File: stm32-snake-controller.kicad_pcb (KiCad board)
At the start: 4 copper layers, 100 x 72 mm, 84 parts, among them J101 Barrel_Jack_MountingPin, J102 Tag Connector, J103 JST 2.54 Header, J301 Conn_01x03, J302 Conn_01x03, J401 Conn_01x07, J402 Conn_01x07, J501 USB_A, J601 8P8C_LED_Shielded, Q101 AO3501A, SW101 SW_SPDT, SW102 SW_Push, U101 USBLC6-2SC6, U102 M24C64-RMN, U103 STM32F446RCTx, U201 XC6220B331MR-G, U301 74AHCT1G125, U302 74AHCT1G125, U501 STMPS2141STR, U601 PCA9615DP, Y101 32.768kHz, Y102 16MHz

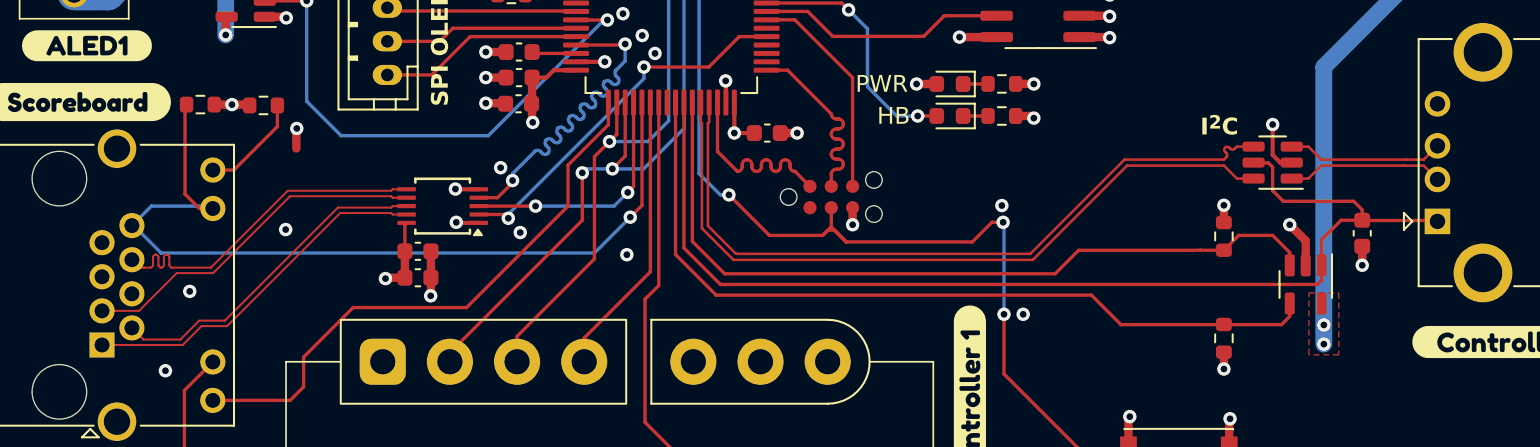
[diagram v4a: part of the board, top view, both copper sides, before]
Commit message: fix differential traces
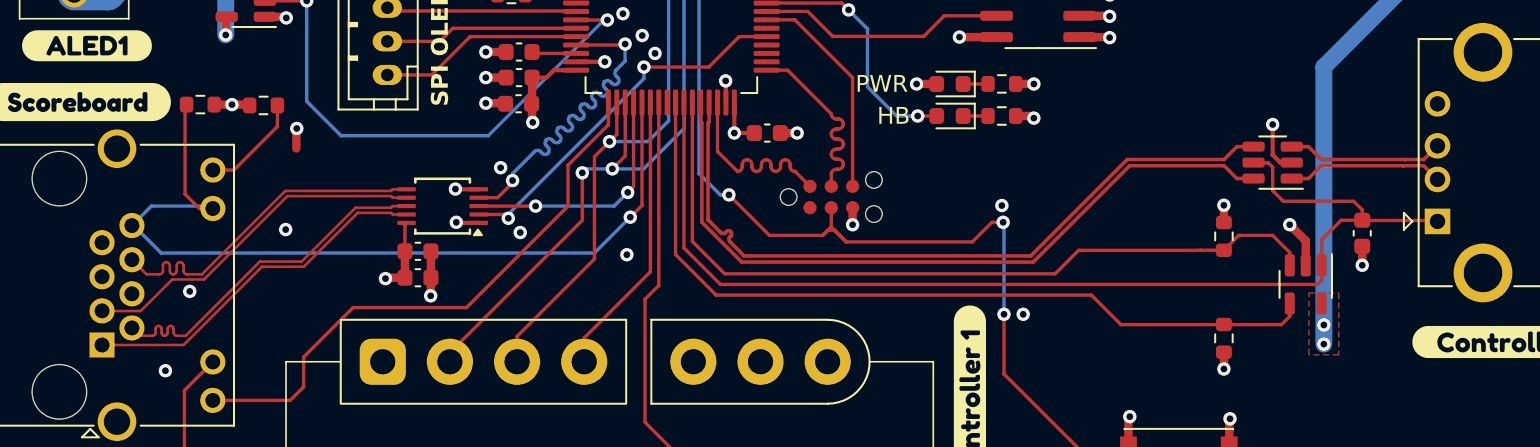
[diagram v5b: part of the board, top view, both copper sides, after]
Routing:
- net /scoreboard/SDA_P: track 19.9 -> 21.4 mm
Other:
- board text added: "0.2104 mm"
- board text added: "1.065 mm"
- board text added: "3.8"
- board text added: "4.4"
- board text added: "7628*1"
- board text added: "Core"
- board text added: "Impedance Notes: Board: JLC04161H-7628 D_P and D_N pairs: 90 ohms (0.2129 width/0.1524 spacing) SDA_P and SDA_N: 100 ohms (0.1547 width/0.1524 spacing) SCL_P and SCL_N: 100 ohms (0.1547 width/0.1524 spacing)"
- board text added: "PCB Stackup: JLC04161H-7628"
- board text removed: "0.0994 mm"
- board text removed: "1.265 mm"
- board text removed: "3.3"
- board text removed: "FR4"
- board text removed: "I^{2}C"
- board text removed: "Impedance Notes: Board: JLC04161H-3313 D_P and D_N pairs: 90 ohms (0.1554 width/0.2032 spacing) SDA_P and SDA_N: 100 ohms (0.1217 width/0.2032 spacing) SCL_P and SCL_N: 100 ohms (0.1217 width/0.2032 spacing)"
- board text removed: "PCB Stackup: JLC04161H-3313"

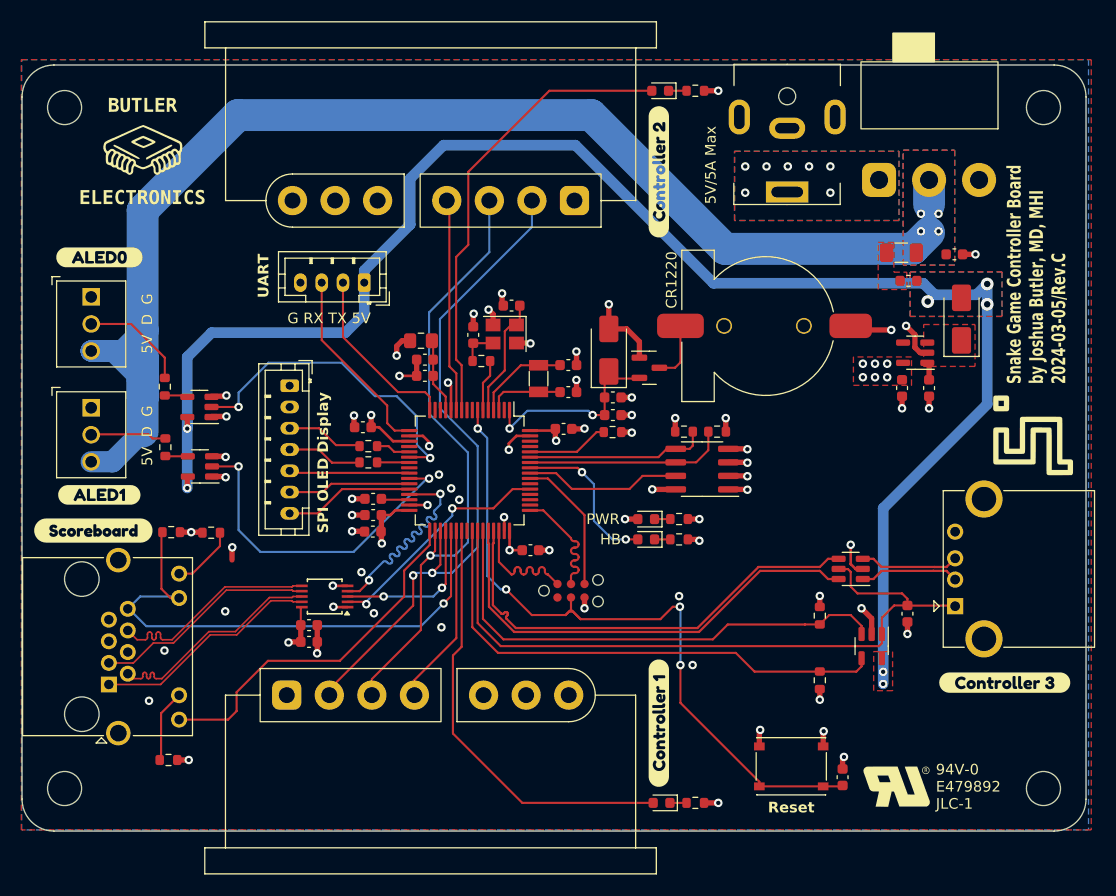
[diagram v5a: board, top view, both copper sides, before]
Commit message: add pull-up resistor for 2nd I2C lines
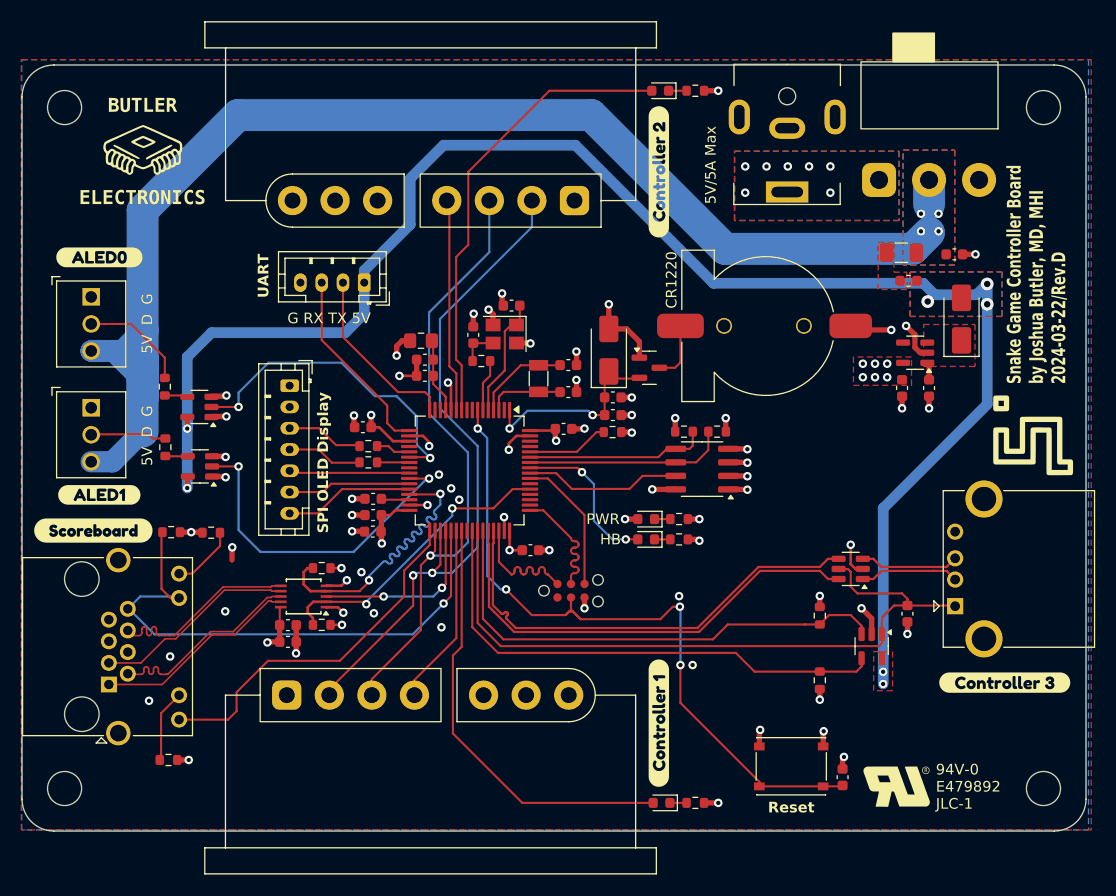
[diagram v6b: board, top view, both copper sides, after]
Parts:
- added R111: 1K5, Resistor_SMD:R_0603_1608Metric, F.Cu at (165.2, 116.6)
- added R112: 1K5, Resistor_SMD:R_0603_1608Metric, F.Cu at (165.2, 111.3)
- moved C601 1.98 mm to (162.0, 118.2)
- moved C602 1.98 mm to (162.0, 116.6)
- moved U601 1.98 mm to (163.5, 114.0)
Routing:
- net /SB_SCL: track 22.0 -> 28.6 mm
- net /SB_SDA: track 22.3 -> 28.1 mm
- net +3V3: track 44.0 -> 46.7 mm, vias 22 -> 24
- net /scoreboard/SDA_P: track 21.4 -> 19.4 mm
- net /scoreboard/SCL_P: track 21.0 -> 19.0 mm
- net /scoreboard/SDA_N: track 21.4 -> 19.5 mm
- net /SB_EN: track 14.7 -> 16.7 mm
- net /scoreboard/SCL_N: track 20.9 -> 19.0 mm
- net GND: track 77.0 -> 77.7 mm
- net /SB_LINK: track 51.1 -> 51.7 mm

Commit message: update silkscreen
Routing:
- added copper zone on In2.Cu, net +3V3
- added copper zone on B.Cu, net GND
- removed copper zone on B.Cu, net +3V3
- removed copper zone on In2.Cu, net GND
